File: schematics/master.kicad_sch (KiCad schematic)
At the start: 26 parts, among them M2 Motor, M3 Motor, Q1 TLE5206_2S, Q2 TLE5206_2S, SW5 Reset, U10 PIC32MX170F256B, U5 Tape_Left, U6 Tape_Middle, U7 Tape_Right, U8 Quadrature_Encoder, U9 Quadrature_Encoder

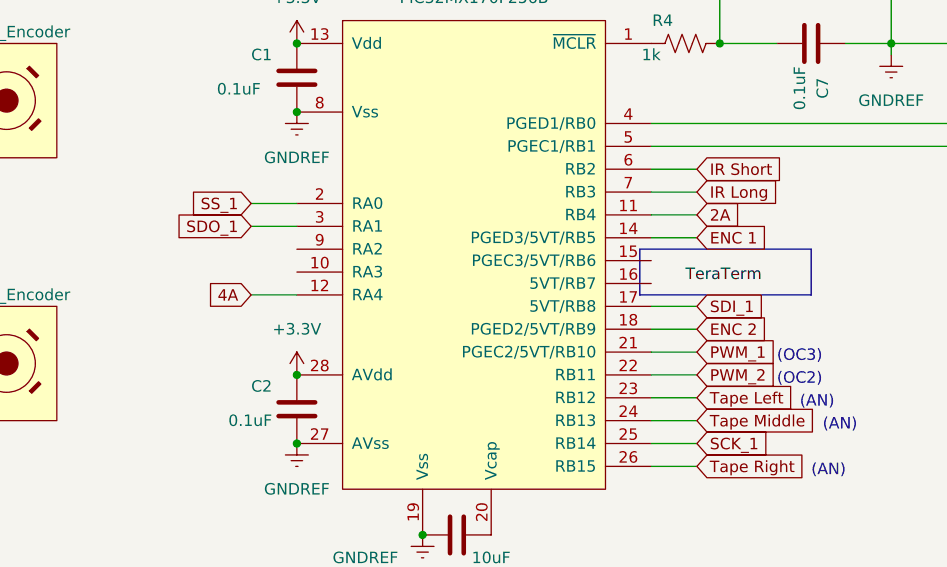
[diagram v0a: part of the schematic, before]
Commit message: Choose encoder pins and correct rollover time update.
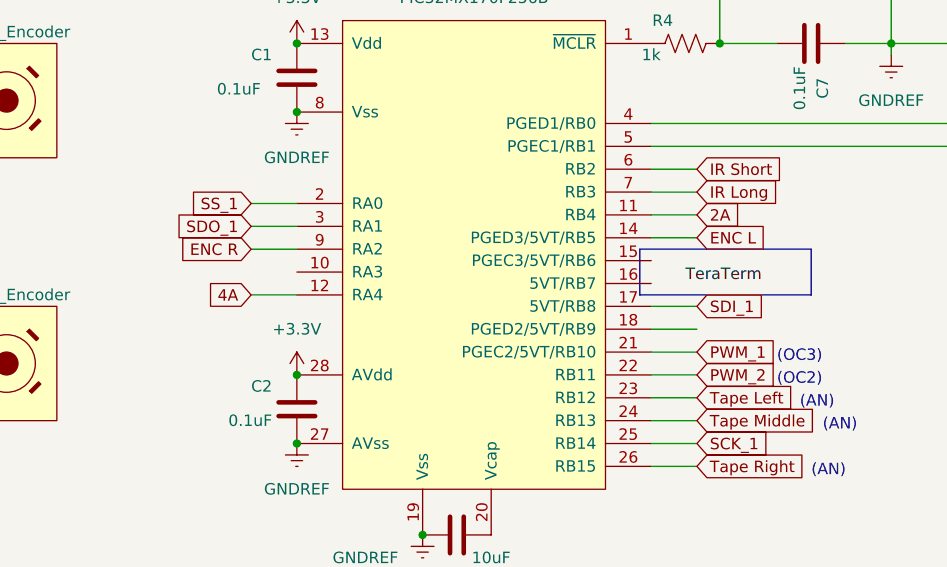
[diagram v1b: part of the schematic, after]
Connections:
- net ENC 1: no longer U10.14 (PGED3/5VT/RB5)
- net ENC 2: no longer U10.18 (PGED2/5VT/RB9)
- net ENC R: now reaches U10.9 (RA2)
- new net ENC L: U10.14 (PGED3/5VT/RB5)
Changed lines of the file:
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@@
+    (stroke (width 0) (type default) (color 0 0 0 0))
+  )
+  (wire (pts (xy 167.64 58.42) (xy 172.72 58.42))
     (stroke (width 0) (type default) (color 0 0 0 0))
   )
@@
     )
   )
-  (global_label "ENC 2" (shape input) (at 217.17 67.31 0) (fields_autoplaced)
-    (effects (font (size 1.27 1.27)) (justify left))
-    (property "Intersheet References" "${INTERSHEET_REFS}" (id 0) (at 225.5098 67.3894 0)
-      (effects (font (size 1.27 1.27)) (justify left) hide)
-    )
-  )
-  (global_label "ENC 1" (shape input) (at 217.17 57.15 0) (fields_autoplaced)
-    (effects (font (size 1.27 1.27)) (justify left))
-    (property "Intersheet References" "${INTERSHEET_REFS}" (id 0) (at 225.5098 57.2294 0)
+  (global_label "ENC L" (shape input) (at 217.17 57.15 0) (fields_autoplaced)
+    (effects (font (size 1.27 1.27)) (justify left))
+    (property "Intersheet References" "${INTERSHEET_REFS}" (id 0) (at 225.3283 57.0706 0)
       (effects (font (size 1.27 1.27)) (justify left) hide)
     )
@@
       (effects (font (size 1.27 1.27)) (justify right) hide)
     )
+  )
+  (global_label "ENC R" (shape input) (at 167.64 58.42 180) (fields_autoplaced)
+    (effects (font (size 1.27 1.27)) (justify right))
+    (property "Intersheet References" "${INTERSHEET_REFS}" (id 0) (at 159.2398 58.4994 0)
+      (effects (font (size 1.27 1.27)) (justify right) hide)
+    )
